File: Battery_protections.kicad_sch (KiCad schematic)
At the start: 26 parts, among them J6 thermistor, Q2 SI2102A-TP, Q3 SI2102A-TP, Q4 SI2102A-TP, Q5 SI2102A-TP, Q6 SI2102A-TP, U4 BQ29209DRBR, U5 AP9101CK6, U6 AP9101CK6, U7 LM358

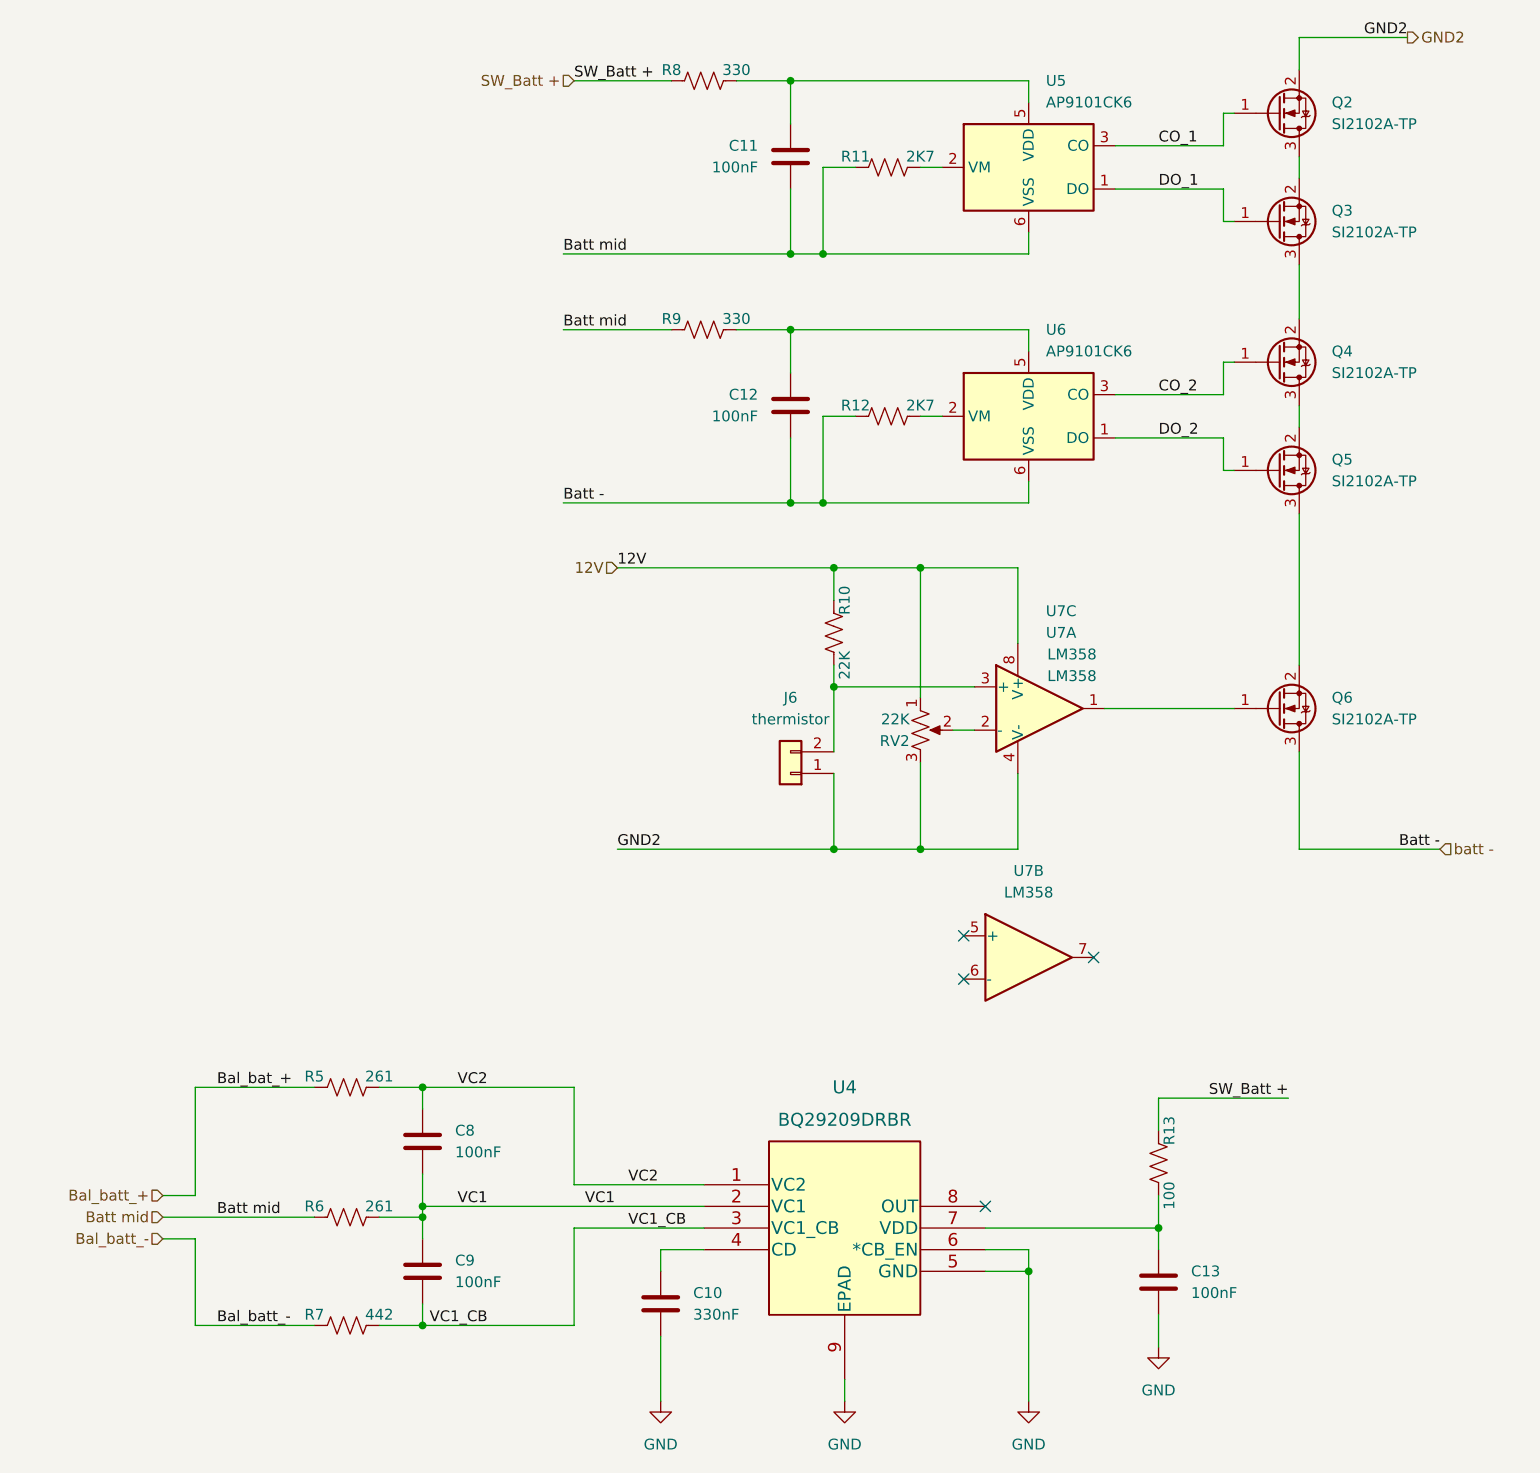
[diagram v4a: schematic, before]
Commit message: layout 1 done, dsr errors with gnd plane clearances
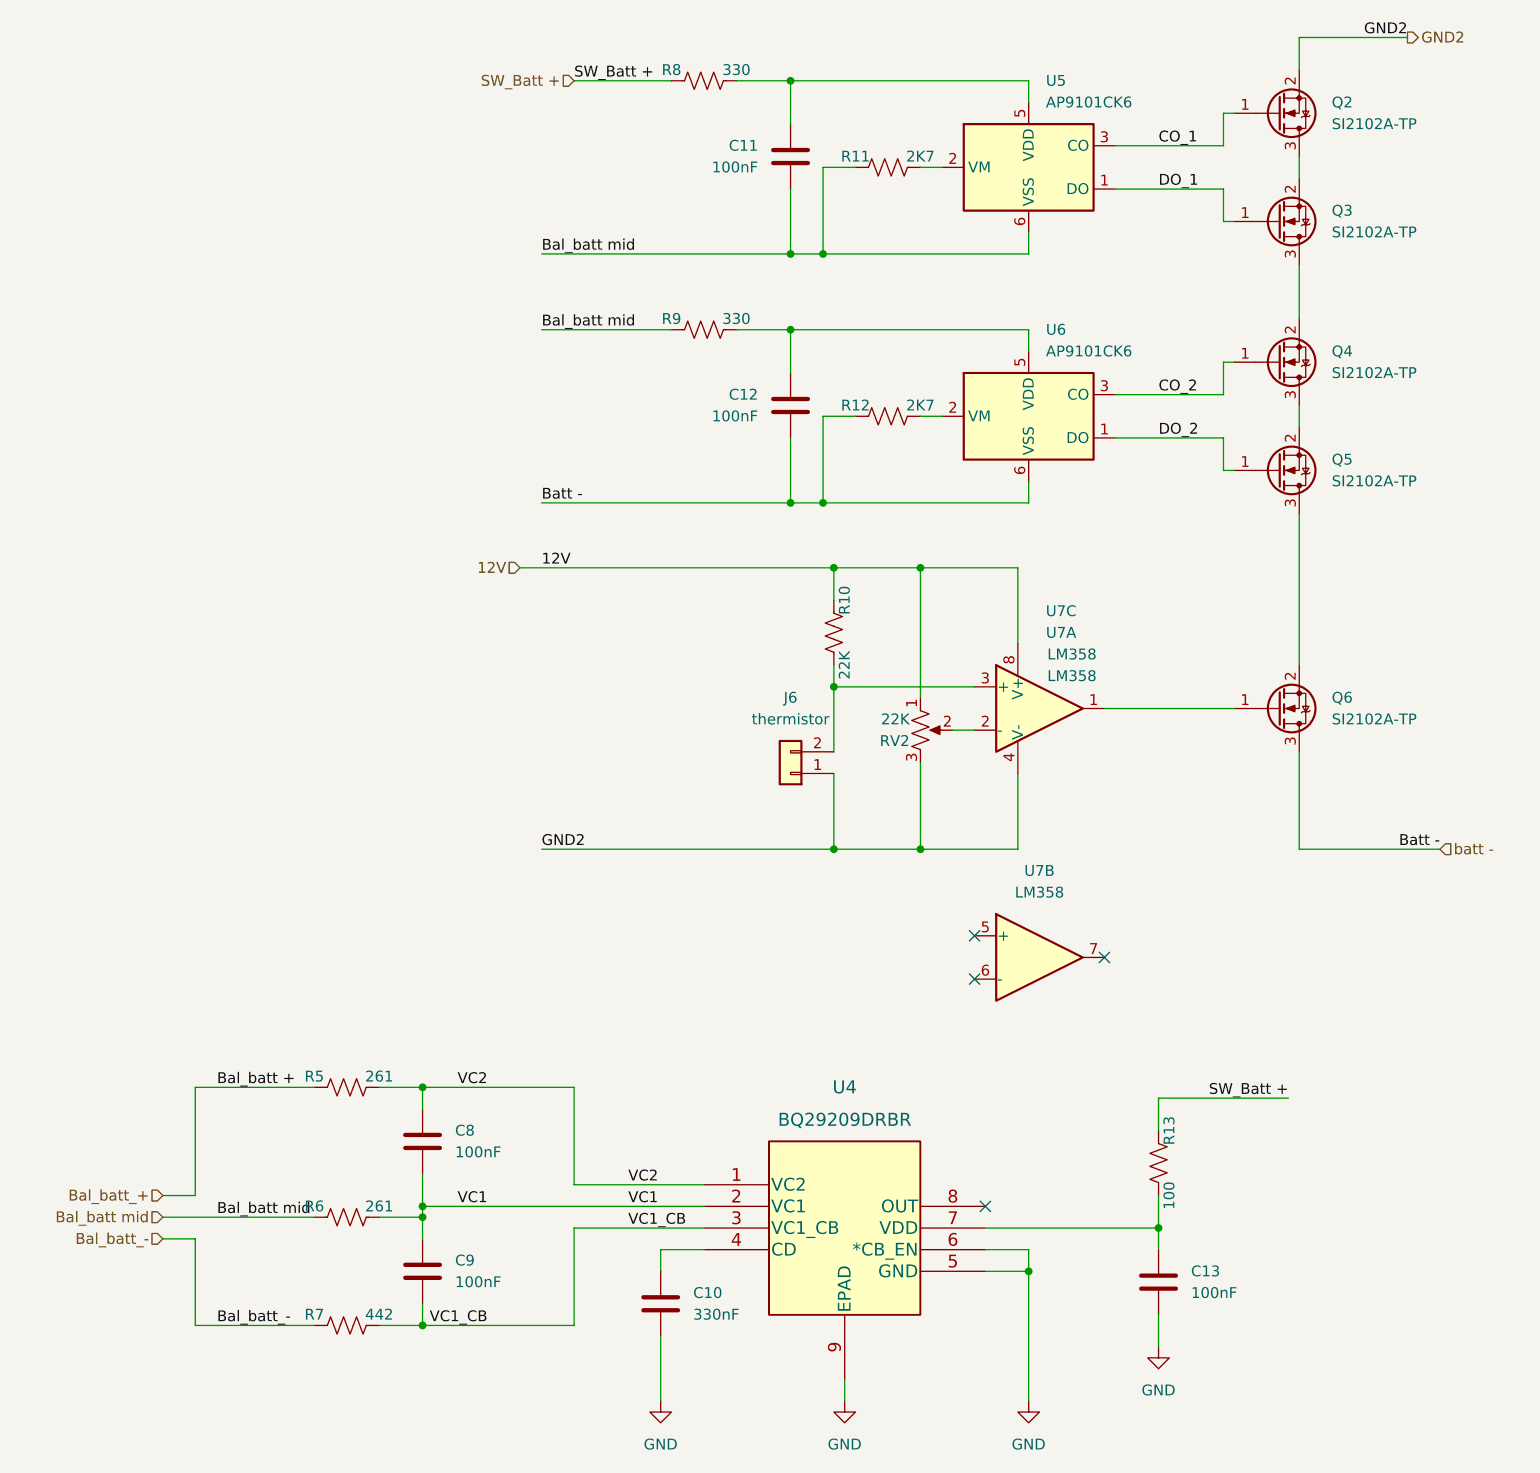
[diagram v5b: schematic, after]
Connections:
- net Batt mid renamed Bal_batt mid
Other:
- moved on the sheet: U7B
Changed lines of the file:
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@@
   (junction (at 110.49 86.36) (diameter 0) (color 0 0 0 0)
   )
-  (no_connect (at 125.73 129.54))
-  (no_connect (at 125.73 134.62))
-  (no_connect (at 140.97 132.08))
+  (no_connect (at 127 129.54))
+  (no_connect (at 127 134.62))
+  (no_connect (at 142.24 132.08))
   (no_connect (at 128.27 161.29))
   (wire (pts (xy 111.76 181.61) (xy 111.76 184.15))
@@
     (stroke (width 0) (type default) (color 0 0 0 0))
   )
-  (wire (pts (xy 78.74 78.74) (xy 105.41 78.74))
+  (wire (pts (xy 76.2 78.74) (xy 105.41 78.74))
     (stroke (width 0) (type default) (color 0 0 0 0))
   )
@@
     (stroke (width 0) (type default) (color 0 0 0 0))
   )
-  (wire (pts (xy 85.09 119.38) (xy 110.49 119.38))
+  (wire (pts (xy 76.2 119.38) (xy 110.49 119.38))
     (stroke (width 0) (type default) (color 0 0 0 0))
   )
@@
     (stroke (width 0) (type default) (color 0 0 0 0))
   )
-  (wire (pts (xy 78.74 58.42) (xy 91.44 58.42))
+  (wire (pts (xy 76.2 58.42) (xy 91.44 58.42))
     (stroke (width 0) (type default) (color 0 0 0 0))
   )
@@
     (stroke (width 0) (type default) (color 0 0 0 0))
   )
-  (wire (pts (xy 85.09 86.36) (xy 110.49 86.36))
+  (wire (pts (xy 73.66 86.36) (xy 110.49 86.36))
     (stroke (width 0) (type default) (color 0 0 0 0))
   )
@@
     (stroke (width 0) (type default) (color 0 0 0 0))
   )
-  (wire (pts (xy 78.74 49.53) (xy 105.41 49.53))
+  (wire (pts (xy 76.2 49.53) (xy 105.41 49.53))
     (stroke (width 0) (type default) (color 0 0 0 0))
   )
@@
     (stroke (width 0) (type default) (color 0 0 0 0))
   )
-  (label "Batt mid" (at 78.74 49.53 0)
+  (label "Bal_batt mid" (at 76.2 49.53 0)
     (effects (font (size 1.27 1.27)) (justify left bottom))
   )
@@
     (effects (font (size 1.27 1.27)) (justify left bottom))
   )
-  (label "Batt mid" (at 78.74 58.42 0)
+  (label "Bal_batt mid" (at 76.2 58.42 0)
     (effects (font (size 1.27 1.27)) (justify left bottom))
   )
@@
     (effects (font (size 1.27 1.27)) (justify right bottom))
   )
-  (label "VC1" (at 81.28 161.29 0)
+  (label "VC1" (at 86.36 161.29 0)
     (effects (font (size 1.27 1.27)) (justify left bottom))
   )
@@
     (effects (font (size 1.27 1.27)) (justify left bottom))
   )
-  (label "Batt -" (at 78.74 78.74 0)
+  (label "Batt -" (at 76.2 78.74 0)
     (effects (font (size 1.27 1.27)) (justify left bottom))
   )
@@
     (effects (font (size 1.27 1.27)) (justify left bottom))
   )
-  (label "Batt mid" (at 38.1 162.56 0)
-    (effects (font (size 1.27 1.27)) (justify left bottom))
-  )
-  (label "Bal_bat_+" (at 38.1 147.32 0)
+  (label "Bal_batt mid" (at 38.1 162.56 0)
+    (effects (font (size 1.27 1.27)) (justify left bottom))
+  )
+  (label "Bal_batt +" (at 38.1 147.32 0)
     (effects (font (size 1.27 1.27)) (justify left bottom))
   )
@@
     (effects (font (size 1.27 1.27)) (justify right bottom))
   )
-  (label "GND2" (at 85.09 119.38 0)
+  (label "GND2" (at 76.2 119.38 0)
     (effects (font (size 1.27 1.27)) (justify left bottom))
   )
@@
     (effects (font (size 1.27 1.27)) (justify left bottom))
   )
-  (label "12V" (at 85.09 86.36 0)
+  (label "12V" (at 76.2 86.36 0)
     (effects (font (size 1.27 1.27)) (justify left bottom))
   )
@@
     (effects (font (size 1.27 1.27)) (justify right))
   )
-  (hierarchical_label "Batt mid" (shape input) (at 31.75 162.56 180)
+  (hierarchical_label "Bal_batt mid" (shape input) (at 31.75 162.56 180)
     (effects (font (size 1.27 1.27)) (justify right))
   )
@@
     (effects (font (size 1.27 1.27)) (justify left))
   )
-  (hierarchical_label "12V" (shape input) (at 85.09 86.36 180)
+  (hierarchical_label "12V" (shape input) (at 73.66 86.36 180)
     (effects (font (size 1.27 1.27)) (justify right))
   )
@@
     (pin "8")
   )
-  (symbol (lib_id "Amplifier_Operational:LM358") (at 133.35 132.08 0) (unit 2)
-    (in_bom yes) (on_board yes) (fields_autoplaced)
-    (property "Reference" "U7" (id 0) (at 133.35 121.92 0))
-    (property "Value" "LM358" (id 1) (at 133.35 124.46 0))
-    (property "Footprint" "Package_DIP:DIP-8_W7.62mm_LongPads" (id 2) (at 133.35 132.08 0)
-      (effects (font (size 1.27 1.27)) hide)
-    )
-    (property "Datasheet" "http://www.ti.com/lit/ds/symlink/lm2904-n.pdf" (id 3) (at 133.35 132.08 0)
-      (effects (font (size 1.27 1.27)) hide)
-    )
+  (symbol (lib_id "Amplifier_Operational:LM358") (at 134.62 132.08 0) (unit 2)
+    (in_bom yes) (on_board yes) (fields_autoplaced)
+    (property "Reference" "U7" (id 0) (at 134.62 121.92 0))
+    (property "Value" "LM358" (id 1) (at 134.62 124.46 0))
+    (property "Footprint" "Package_DIP:DIP-8_W7.62mm_LongPads" (id 2) (at 134.62 132.08 0)
+      (effects (font (size 1.27 1.27)) hide)
+    )
+    (property "Datasheet" "http://www.ti.com/lit/ds/symlink/lm2904-n.pdf" (id 3) (at 134.62 132.08 0)
+      (effects (font (size 1.27 1.27)) hide)
+    )

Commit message: 1st Gerber creatd  Please enter the commit message for your changes. Lines starting
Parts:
- renumbered C9 to C10, C10 to C11, C11 to C12, C12 to C13, C13 to C14, C8 to C9
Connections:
- net batt -: now also Q6.2 (S); no longer Q6.3 (D)
- net at Q4.2 (S): now also Q3.2 (S); no longer Q3.3 (D)
- net at Q4.3 (D): now also Q5.3 (D); no longer Q5.2 (S)
- net at Q2.3 (D): now also Q3.3 (D); no longer Q3.2 (S)
- new net: Q5.2 (S), Q6.3 (D)
